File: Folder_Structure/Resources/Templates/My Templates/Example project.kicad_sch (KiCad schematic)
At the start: 0 parts

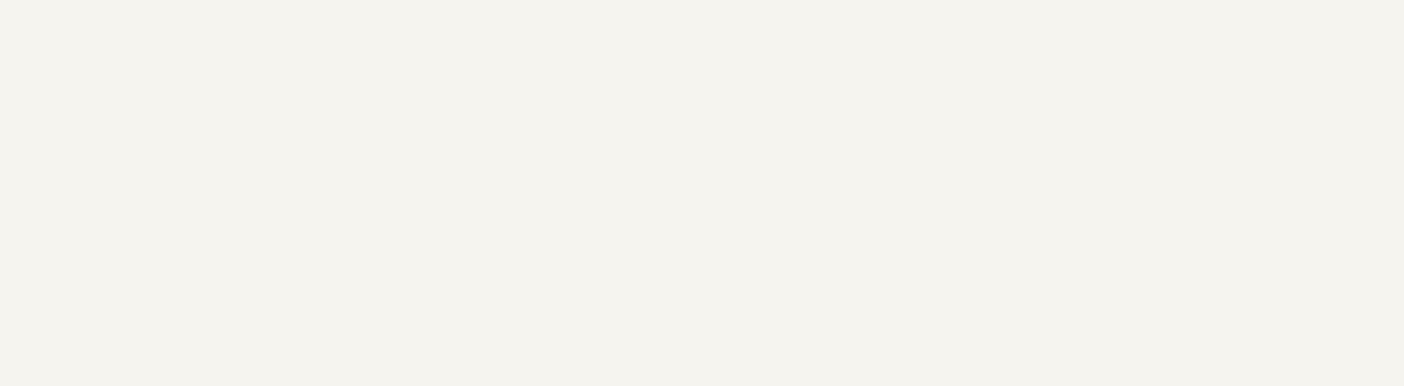
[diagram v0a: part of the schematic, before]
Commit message: updated the template
schematic is updated as a template for future use
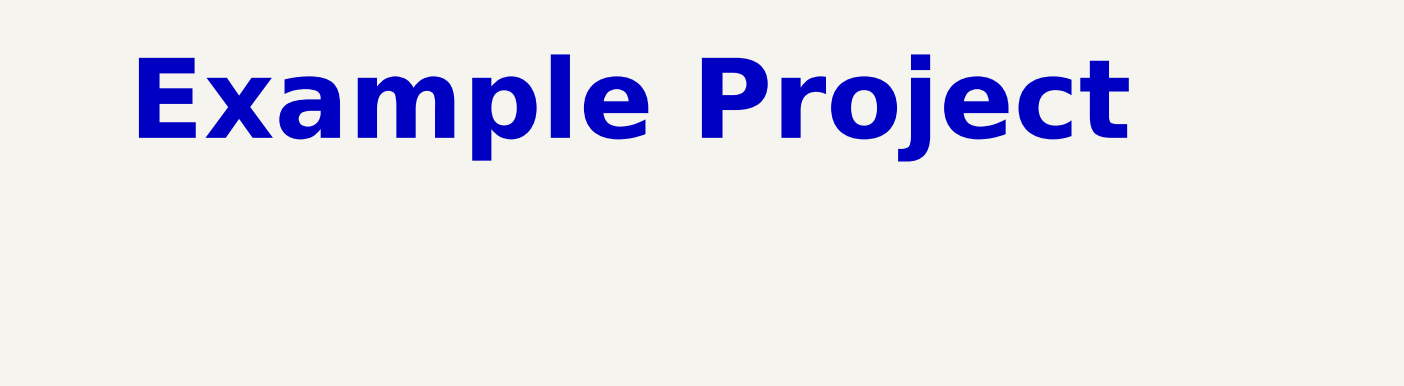
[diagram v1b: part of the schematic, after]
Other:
- note added: "${TITLE}"
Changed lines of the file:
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@@
+		)
+	)
+	(text "${TITLE}"
+		(exclude_from_sim no)
+		(at 131.064 23.622 0)
+		(effects
+			(font
+				(size 8.89 8.89)
+				(thickness 1.778)
+				(bold yes)
+			)
 		)
 	)
